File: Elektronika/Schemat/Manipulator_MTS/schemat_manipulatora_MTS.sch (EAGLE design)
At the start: 10 parts, among them IC1 MODUL_POLOLU, U1 PRZETWORNICA

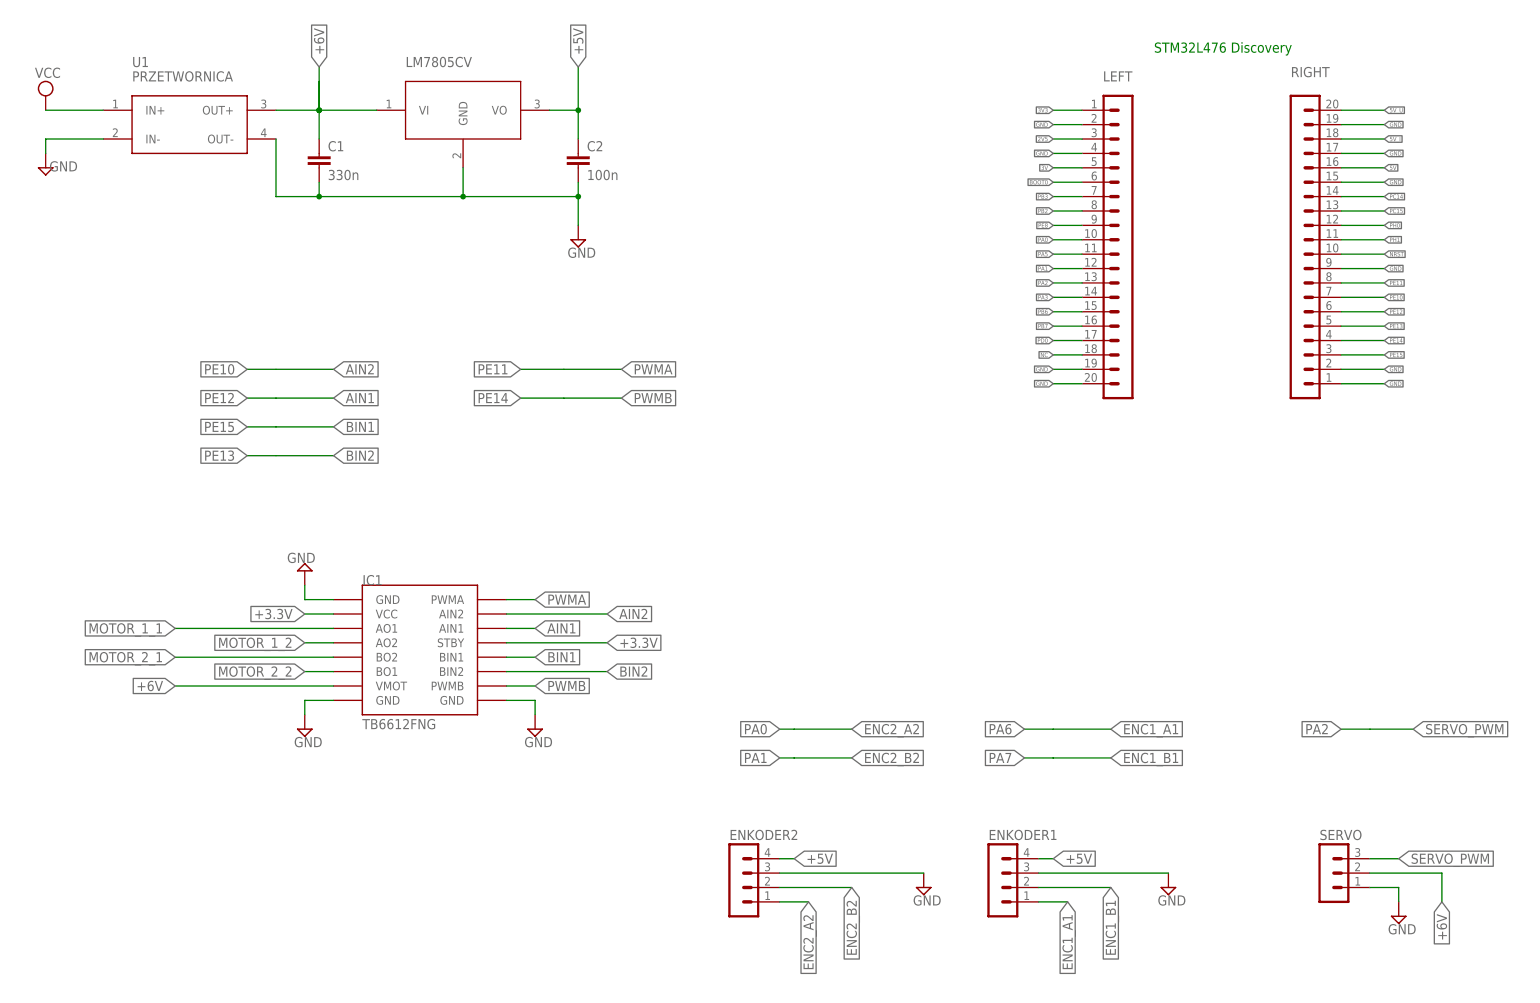
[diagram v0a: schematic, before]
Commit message: v0.1.1
Dodano:
- dokumentację płytki STM32L476VG Discovery
- projekt płytki PCB
- poprawiono kofigurację mikrokotrolera
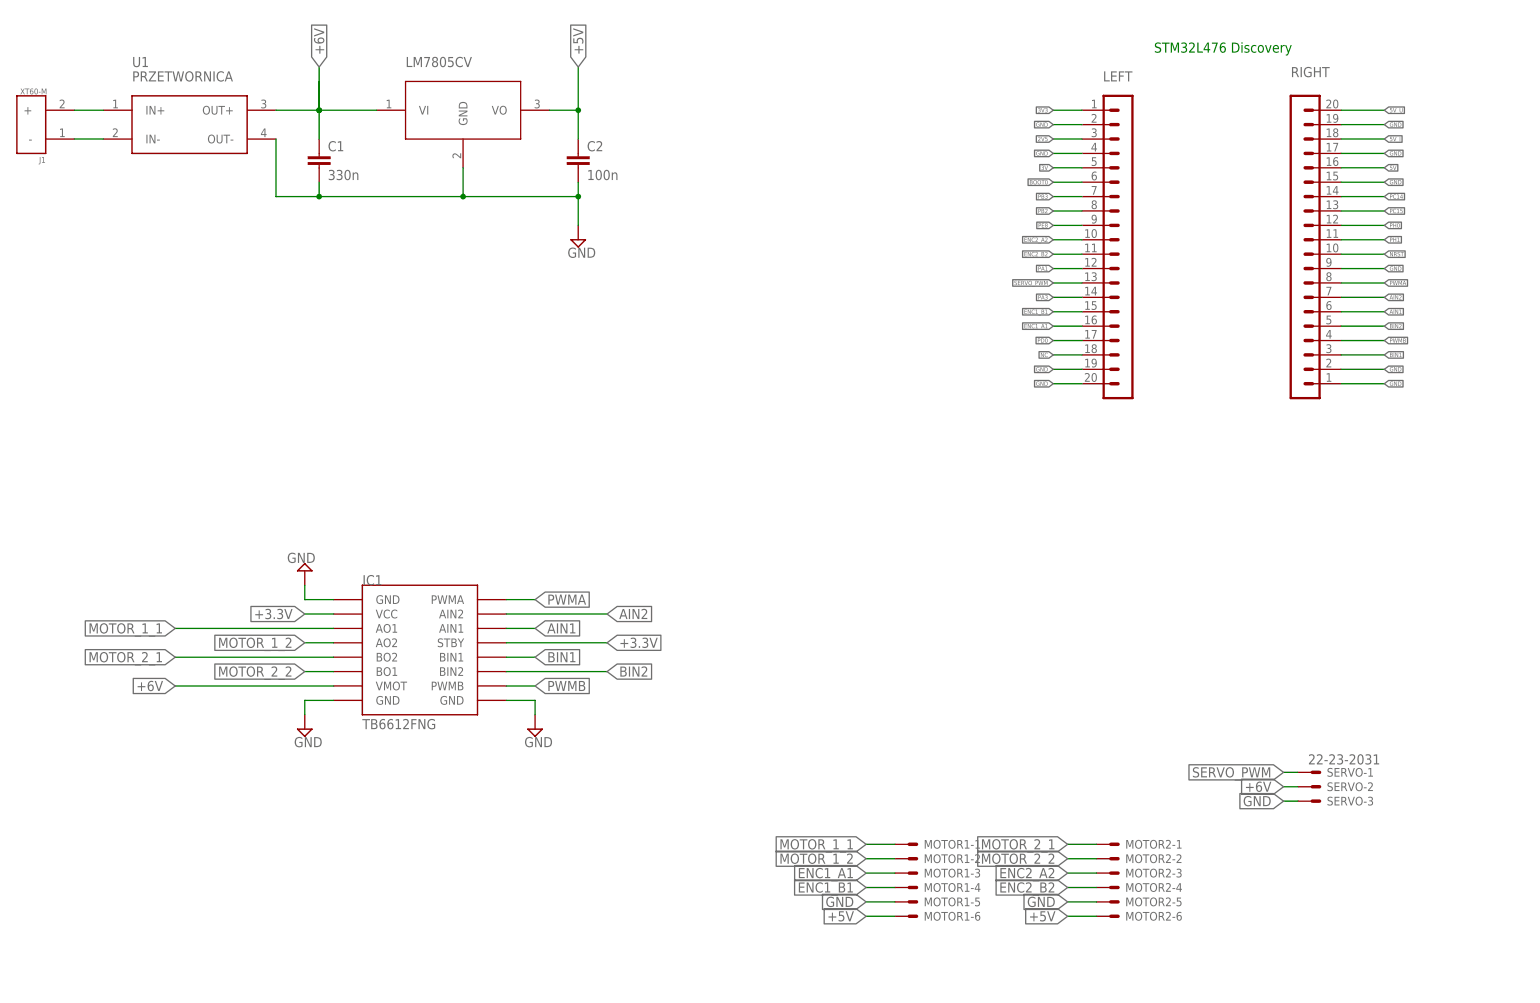
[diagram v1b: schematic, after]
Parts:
- removed ENKODER1, ENKODER2: (no value), con-lstb:MA04-1
- added J1: XT60-M, XT60-M:XT60-M
- added MOTOR1, MOTOR2: (no value), con-molex:22-23-2061
- SERVO: value (none) -> 22-23-2031; device con-lstb:MA03-1 -> con-molex:22-23-2031
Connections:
- removed net PA0: LEFT.10
- removed net PA2: LEFT.13
- removed net PA5: LEFT.11
- removed net PB6: LEFT.15
- removed net PB7: LEFT.16
- removed net PE10: RIGHT.7
- removed net PE11: RIGHT.8
- removed net PE12: RIGHT.6
- removed net PE13: RIGHT.5
- removed net PE14: RIGHT.4
- removed net PE15: RIGHT.3
- removed net VCC: U1.IN+
- new net N$1: J1.+, U1.IN+
- new net N$2: J1.-, U1.IN-
- net +5V: now also MOTOR1-6.S, MOTOR2-6.S; no longer ENKODER1.4, ENKODER2.4
- net +6V: now also SERVO-2.S; no longer SERVO.2
- net AIN1: now also RIGHT.6
- net AIN2: now also RIGHT.7
- net BIN1: now also RIGHT.3
- net BIN2: now also RIGHT.5
- net ENC1_A1: now also LEFT.16, MOTOR1-3.S; no longer ENKODER1.1
- net ENC1_B1: now also LEFT.15, MOTOR1-4.S; no longer ENKODER1.2
- net ENC2_A2: now also LEFT.10, MOTOR2-3.S; no longer ENKODER2.1
- net ENC2_B2: now also LEFT.11, MOTOR2-4.S; no longer ENKODER2.2
- net GND: now also MOTOR1-5.S, MOTOR2-5.S, SERVO-3.S; no longer ENKODER1.3, ENKODER2.3, SERVO.1, U1.IN-
- net MOTOR_1_1: now also MOTOR1-1.S
- net MOTOR_1_2: now also MOTOR1-2.S
- net MOTOR_2_1: now also MOTOR2-1.S
- net MOTOR_2_2: now also MOTOR2-2.S
- net PWMA: now also RIGHT.8
- net PWMB: now also RIGHT.4
- net SERVO_PWM: now also LEFT.13, SERVO-1.S; no longer SERVO.3

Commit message: v0.1.1
Dodano:
- w pełni stworzony model płytki PCB
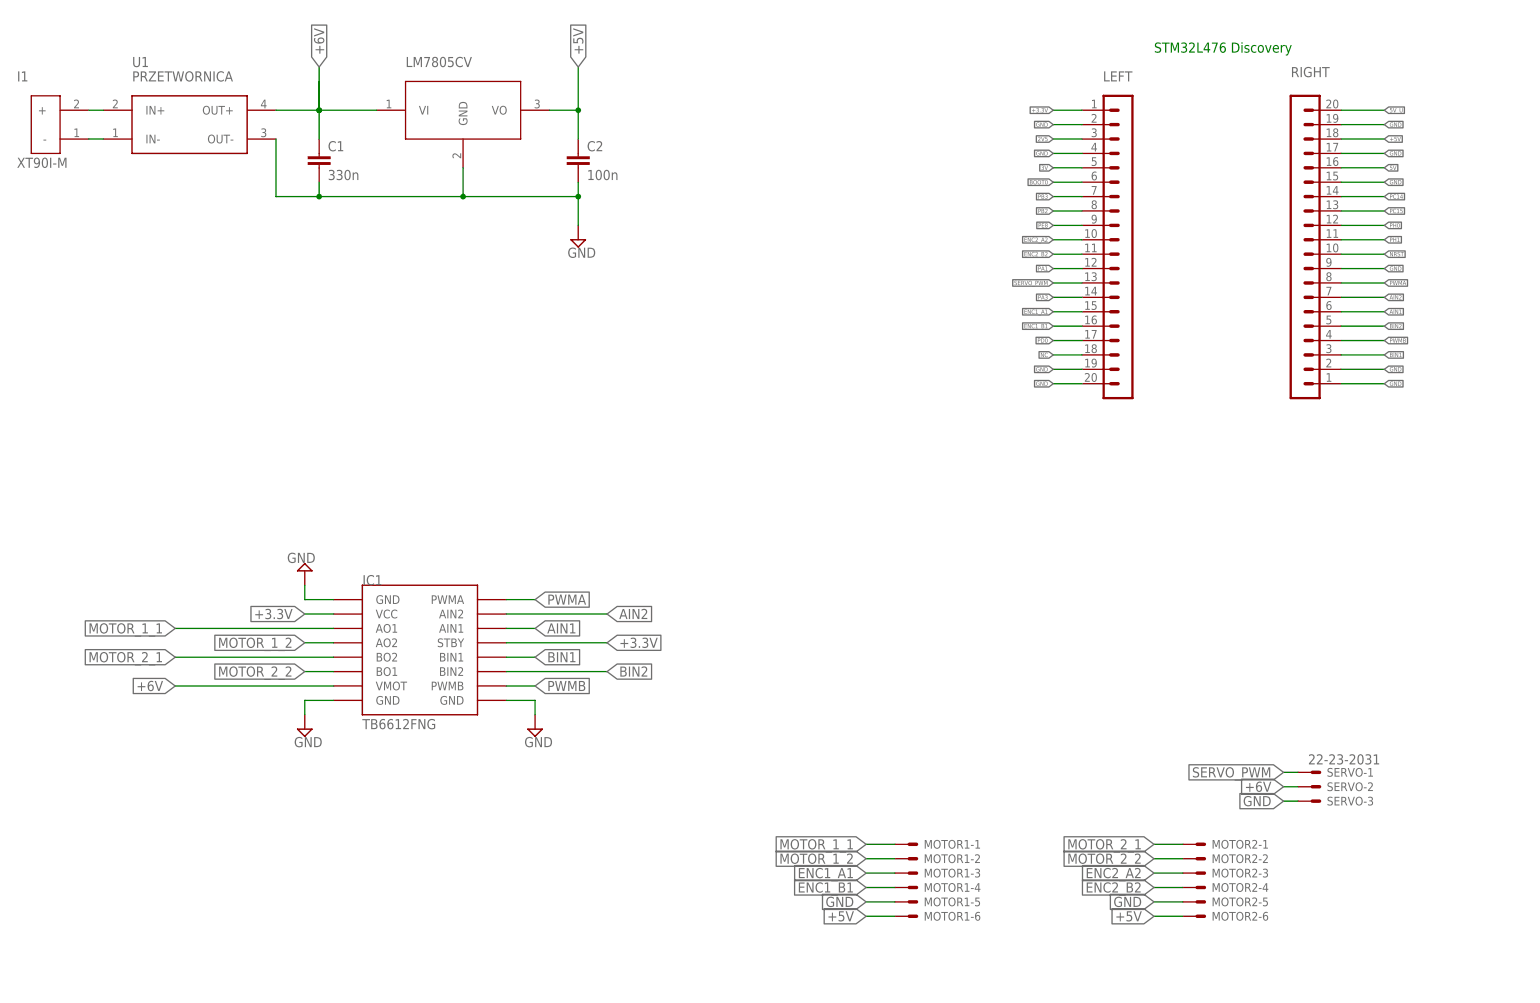
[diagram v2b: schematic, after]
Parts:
- removed J1: XT60-M, XT60-M:XT60-M
- added I1: XT90I-M, amy_library:XT90I-M
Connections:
- removed net 3V3: LEFT.1
- removed net 5V_I: RIGHT.18
- net +3.3V: now also LEFT.1
- net +5V: now also RIGHT.18
- net ENC1_A1: now also LEFT.15; no longer LEFT.16
- net ENC1_B1: now also LEFT.16; no longer LEFT.15
- net N$1: now also I1.+; no longer J1.+
- net N$2: now also I1.-; no longer J1.-
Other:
- moved on the sheet: MOTOR2-1, MOTOR2-2, MOTOR2-3, MOTOR2-4, MOTOR2-5, MOTOR2-6
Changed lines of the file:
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@@
 <part name="MOTOR2" library="con-molex" library_urn="urn:adsk.eagle:library:165" deviceset="22-23-2061" device="" package3d_urn="urn:adsk.eagle:package:8078637/1"/>
 <part name="SERVO" library="con-molex" library_urn="urn:adsk.eagle:library:165" deviceset="22-23-2031" device="" package3d_urn="urn:adsk.eagle:package:8078634/1"/>
-<part name="J1" library="XT60-M" deviceset="XT60-M" device=""/>
+<part name="I1" library="amy_library" deviceset="XT90I-M" device=""/>
 </parts>
 <sheets>
@@
 <attribute name="NAME" x="167.64" y="29.718" size="1.524" layer="95"/>
 </instance>
-<instance part="MOTOR2" gate="-1" x="200.66" y="43.18" smashed="yes">
-<attribute name="NAME" x="203.2" y="42.418" size="1.524" layer="95"/>
-<attribute name="VALUE" x="199.898" y="44.577" size="1.778" layer="96"/>
-</instance>
-<instance part="MOTOR2" gate="-2" x="200.66" y="40.64" smashed="yes">
-<attribute name="NAME" x="203.2" y="39.878" size="1.524" layer="95"/>
-</instance>
-<instance part="MOTOR2" gate="-3" x="200.66" y="38.1" smashed="yes">
-<attribute name="NAME" x="203.2" y="37.338" size="1.524" layer="95"/>
-</instance>
-<instance part="MOTOR2" gate="-4" x="200.66" y="35.56" smashed="yes">
-<attribute name="NAME" x="203.2" y="34.798" size="1.524" layer="95"/>
-</instance>
-<instance part="MOTOR2" gate="-5" x="200.66" y="33.02" smashed="yes">
-<attribute name="NAME" x="203.2" y="32.258" size="1.524" layer="95"/>
-</instance>
-<instance part="MOTOR2" gate="-6" x="200.66" y="30.48" smashed="yes">
-<attribute name="NAME" x="203.2" y="29.718" size="1.524" layer="95"/>
+<instance part="MOTOR2" gate="-1" x="215.9" y="43.18" smashed="yes">
+<attribute name="NAME" x="218.44" y="42.418" size="1.524" layer="95"/>
+<attribute name="VALUE" x="215.138" y="44.577" size="1.778" layer="96"/>
+</instance>
+<instance part="MOTOR2" gate="-2" x="215.9" y="40.64" smashed="yes">
+<attribute name="NAME" x="218.44" y="39.878" size="1.524" layer="95"/>
+</instance>
+<instance part="MOTOR2" gate="-3" x="215.9" y="38.1" smashed="yes">
+<attribute name="NAME" x="218.44" y="37.338" size="1.524" layer="95"/>
+</instance>
+<instance part="MOTOR2" gate="-4" x="215.9" y="35.56" smashed="yes">
+<attribute name="NAME" x="218.44" y="34.798" size="1.524" layer="95"/>
+</instance>
+<instance part="MOTOR2" gate="-5" x="215.9" y="33.02" smashed="yes">
+<attribute name="NAME" x="218.44" y="32.258" size="1.524" layer="95"/>
+</instance>
+<instance part="MOTOR2" gate="-6" x="215.9" y="30.48" smashed="yes">
+<attribute name="NAME" x="218.44" y="29.718" size="1.524" layer="95"/>
 </instance>
 <instance part="SERVO" gate="-1" x="236.22" y="55.88" smashed="yes">
@@
 <attribute name="NAME" x="238.76" y="50.038" size="1.524" layer="95"/>
 </instance>
-<instance part="J1" gate="G$1" x="10.16" y="170.18" smashed="yes" rot="R180">
-<attribute name="NAME" x="12.70485" y="164.454090625" size="1.017940625" layer="95" rot="R180"/>
-<attribute name="VALUE" x="12.95893125" y="176.541209375" size="1.017790625" layer="96" rot="R180"/>
+<instance part="I1" gate="TX90I-M" x="12.7" y="170.18" smashed="yes">
+<attribute name="NAME" x="7.62" y="177.8" size="1.778" layer="95"/>
+<attribute name="VALUE" x="7.62" y="162.56" size="1.778" layer="96"/>
 </instance>
 </instances>
@@
 <segment>
 <pinref part="MOTOR2" gate="-5" pin="S"/>
-<wire x1="198.12" y1="33.02" x2="193.04" y2="33.02" width="0.1524" layer="91"/>
-<label x="193.04" y="33.02" size="1.778" layer="95" rot="R180" xref="yes"/>
+<wire x1="213.36" y1="33.02" x2="208.28" y2="33.02" width="0.1524" layer="91"/>
+<label x="208.28" y="33.02" size="1.778" layer="95" rot="R180" xref="yes"/>
 </segment>
 <segment>
@@
 <segment>
 <pinref part="MOTOR2" gate="-1" pin="S"/>
-<wire x1="198.12" y1="43.18" x2="193.04" y2="43.18" width="0.1524" layer="91"/>
-<label x="193.04" y="43.18" size="1.778" layer="95" rot="R180" xref="yes"/>
+<wire x1="213.36" y1="43.18" x2="208.28" y2="43.18" width="0.1524" layer="91"/>
+<label x="208.28" y="43.18" size="1.778" layer="95" rot="R180" xref="yes"/>
 </segment>
 </net>
@@
 <segment>
 <pinref part="MOTOR2" gate="-2" pin="S"/>
-<wire x1="198.12" y1="40.64" x2="193.04" y2="40.64" width="0.1524" layer="91"/>
-<label x="193.04" y="40.64" size="1.778" layer="95" rot="R180" xref="yes"/>
+<wire x1="213.36" y1="40.64" x2="208.28" y2="40.64" width="0.1524" layer="91"/>
+<label x="208.28" y="40.64" size="1.778" layer="95" rot="R180" xref="yes"/>
 </segment>
 </net>
@@
 <segment>
 <pinref part="MOTOR2" gate="-4" pin="S"/>
-<wire x1="198.12" y1="35.56" x2="193.04" y2="35.56" width="0.1524" layer="91"/>
-<label x="193.04" y="35.56" size="1.778" layer="95" rot="R180" xref="yes"/>
+<wire x1="213.36" y1="35.56" x2="208.28" y2="35.56" width="0.1524" layer="91"/>
+<label x="208.28" y="35.56" size="1.778" layer="95" rot="R180" xref="yes"/>
 </segment>
 </net>
@@
 <segment>
 <pinref part="MOTOR2" gate="-3" pin="S"/>
-<wire x1="198.12" y1="38.1" x2="193.04" y2="38.1" width="0.1524" layer="91"/>
-<label x="193.04" y="38.1" size="1.778" layer="95" rot="R180" xref="yes"/>
+<wire x1="213.36" y1="38.1" x2="208.28" y2="38.1" width="0.1524" layer="91"/>
+<label x="208.28" y="38.1" size="1.778" layer="95" rot="R180" xref="yes"/>
 </segment>
 </net>
 <net name="ENC1_B1" class="0">
+<segment>
+<pinref part="MOTOR1" gate="-4" pin="S"/>
+<wire x1="162.56" y1="35.56" x2="157.48" y2="35.56" width="0.1524" layer="91"/>
+<label x="157.48" y="35.56" size="1.778" layer="95" rot="R180" xref="yes"/>
+</segment>
+<segment>
+<pinref part="LEFT" gate="1" pin="16"/>
+<wire x1="195.58" y1="134.62" x2="190.5" y2="134.62" width="0.1524" layer="91"/>
+<label x="190.5" y="134.62" size="0.762" layer="95" rot="R180" xref="yes"/>
+</segment>
+</net>
+<net name="ENC1_A1" class="0">
+<segment>
+<pinref part="MOTOR1" gate="-3" pin="S"/>
+<wire x1="162.56" y1="38.1" x2="157.48" y2="38.1" width="0.1524" layer="91"/>
+<label x="157.48" y="38.1" size="1.778" layer="95" rot="R180" xref="yes"/>
+</segment>
 <segment>
 <pinref part="LEFT" gate="1" pin="15"/>
 <wire x1="195.58" y1="137.16" x2="190.5" y2="137.16" width="0.1524" layer="91"/>
 <label x="190.5" y="137.16" size="0.762" layer="95" rot="R180" xref="yes"/>
-</segment>
-<segment>
-<pinref part="MOTOR1" gate="-4" pin="S"/>
-<wire x1="162.56" y1="35.56" x2="157.48" y2="35.56" width="0.1524" layer="91"/>
-<label x="157.48" y="35.56" size="1.778" layer="95" rot="R180" xref="yes"/>
-</segment>
-</net>
-<net name="ENC1_A1" class="0">
-<segment>
-<pinref part="LEFT" gate="1" pin="16"/>
-<wire x1="195.58" y1="134.62" x2="190.5" y2="134.62" width="0.1524" layer="91"/>
-<label x="190.5" y="134.62" size="0.762" layer="95" rot="R180" xref="yes"/>
-</segment>
-<segment>
-<pinref part="MOTOR1" gate="-3" pin="S"/>
-<wire x1="162.56" y1="38.1" x2="157.48" y2="38.1" width="0.1524" layer="91"/>
-<label x="157.48" y="38.1" size="1.778" layer="95" rot="R180" xref="yes"/>
 </segment>
 </net>
@@
 <segment>
 <pinref part="MOTOR2" gate="-6" pin="S"/>
-<wire x1="198.12" y1="30.48" x2="193.04" y2="30.48" width="0.1524" layer="91"/>
-<label x="193.04" y="30.48" size="1.778" layer="95" rot="R180" xref="yes"/>
+<wire x1="213.36" y1="30.48" x2="208.28" y2="30.48" width="0.1524" layer="91"/>
+<label x="208.28" y="30.48" size="1.778" layer="95" rot="R180" xref="yes"/>
+</segment>
+<segment>
+<pinref part="RIGHT" gate="1" pin="18"/>
+<wire x1="241.3" y1="167.64" x2="248.92" y2="167.64" width="0.1524" layer="91"/>
+<label x="248.92" y="167.64" size="0.762" layer="95" xref="yes"/>
 </segment>
 </net>
@@
 <label x="111.76" y="78.74" size="1.778" layer="95" xref="yes"/>
 </segment>
-</net>
-<net name="3V3" class="0">
 <segment>
 <pinref part="LEFT" gate="1" pin="1"/>
@@
 </segment>
 </net>
-<net name="5V_I" class="0">
-<segment>
-<pinref part="RIGHT" gate="1" pin="18"/>
-<wire x1="241.3" y1="167.64" x2="248.92" y2="167.64" width="0.1524" layer="91"/>
-<label x="248.92" y="167.64" size="0.762" layer="95" xref="yes"/>
-</segment>
-</net>
 <net name="5V" class="0">
 <segment>
@@
 <net name="N$1" class="0">
 <segment>
-<pinref part="J1" gate="G$1" pin="+"/>
 <pinref part="U1" gate="PRZETWORNICA-STEP-DOWN" pin="IN+"/>
-<wire x1="17.78" y1="172.72" x2="22.86" y2="172.72" width="0.1524" layer="91"/>
+<pinref part="I1" gate="TX90I-M" pin="+"/>
+<wire x1="20.32" y1="172.72" x2="22.86" y2="172.72" width="0.1524" layer="91"/>
 </segment>
 </net>
 <net name="N$2" class="0">
 <segment>
-<pinref part="J1" gate="G$1" pin="-"/>
 <pinref part="U1" gate="PRZETWORNICA-STEP-DOWN" pin="IN-"/>
-<wire x1="17.78" y1="167.64" x2="22.86" y2="167.64" width="0.1524" layer="91"/>
+<pinref part="I1" gate="TX90I-M" pin="-"/>
+<wire x1="20.32" y1="167.64" x2="22.86" y2="167.64" width="0.1524" layer="91"/>
 </segment>
 </net>
@@
 </sheet>
 </sheets>
-<errors>
-</errors>
 </schematic>
 </drawing>
